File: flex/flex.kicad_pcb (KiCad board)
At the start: 2 copper layers, 53.3 x 41.5 mm, 18 parts, among them J1 Conn_01x06_Female, J2 Conn_01x03_Female, SW19 SW_Push, SW5 SW_Push, SW9 SW_Push

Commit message: silkscreen and routing
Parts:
- moved D19 1.41 mm to (101.6, 65.3)
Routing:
- net col4: track 28.6 -> 0.00 mm, vias 1 -> 0
- net col3: track 48.3 -> 22.5 mm, vias 2 -> 1
- net col6: track 23.2 -> 0.00 mm, vias 1 -> 0
- net row1: track 76.6 -> 61.5 mm
- net Net-(D2-Pad1): track 80.1 -> 67.4 mm
- net Vcc: track 88.8 -> 85.9 mm
- net Net-(D19-Pad2): track 6.97 -> 5.18 mm
- net col5: track 21.5 -> 20.0 mm
- added copper zone on B.Cu, net Gnd
- added copper zone on F.Cu, net Gnd
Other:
- board text added: "X"
- board text removed: "C4"
- board text removed: "C6"

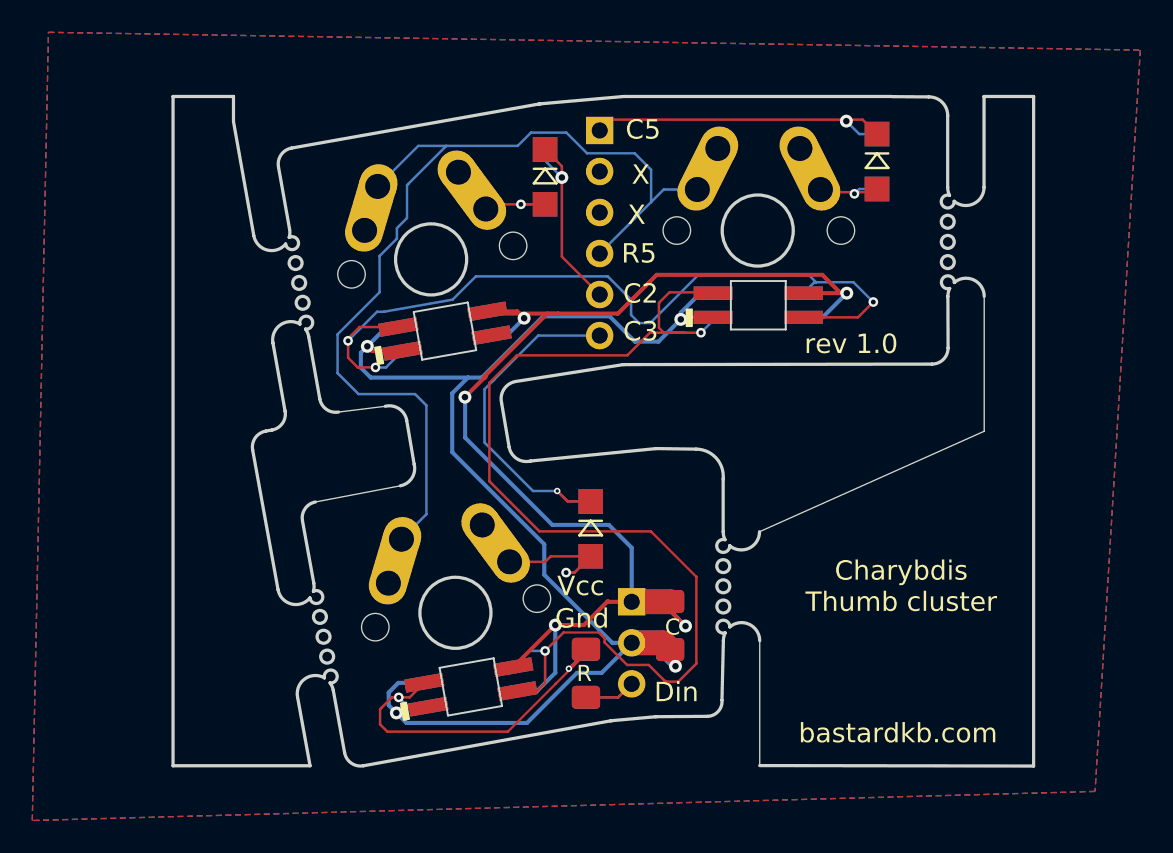
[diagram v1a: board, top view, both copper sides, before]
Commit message: smaller footprint
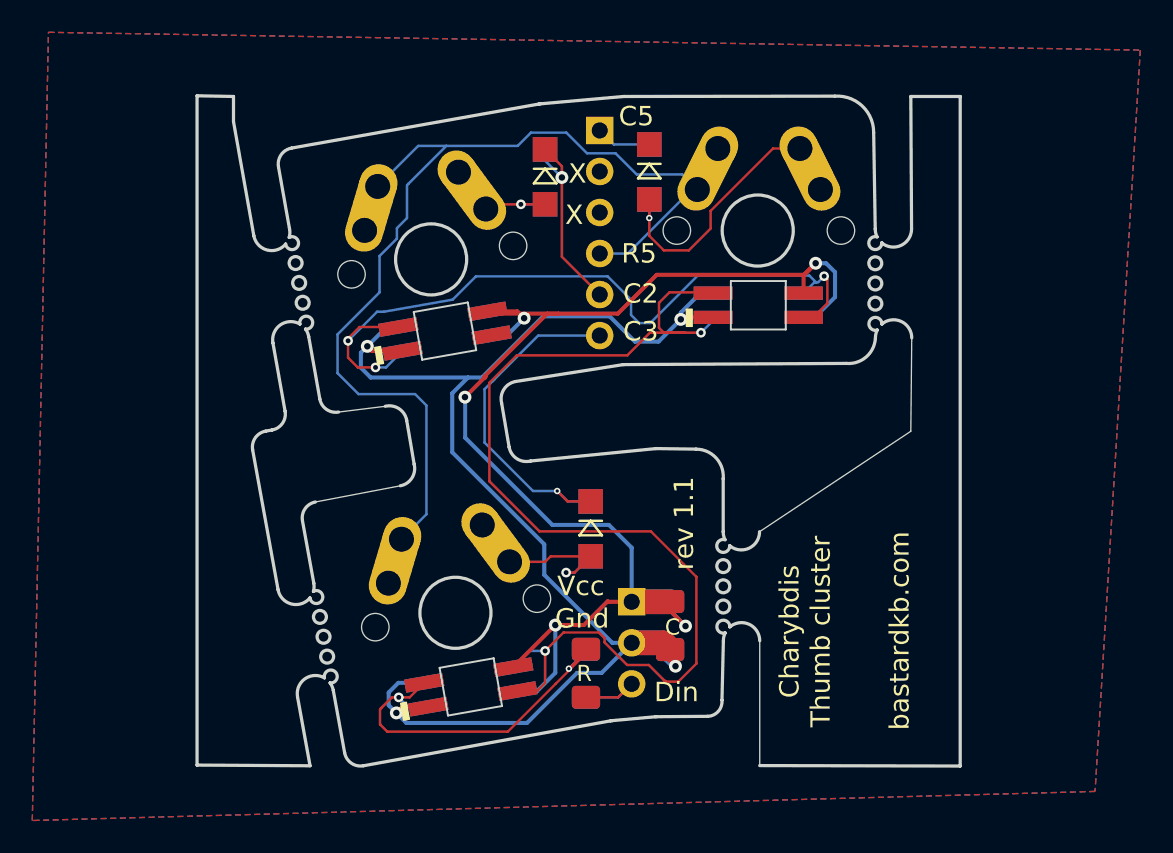
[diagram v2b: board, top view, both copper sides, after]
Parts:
- moved D19 14.1 mm to (87.5, 65.9)
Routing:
- net col5: track 20.0 -> 3.43 mm, vias 1 -> 0
- net Net-(D19-Pad2): track 5.18 -> 16.4 mm
- net Net-(D10-Pad1): track 52.0 -> 47.5 mm
- net row1: track 61.5 -> 62.8 mm
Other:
- board size 53.3 x 41.5 mm -> 47.2 x 41.5 mm
- board text added: "rev 1.1"
- board text removed: "rev 1.0"
